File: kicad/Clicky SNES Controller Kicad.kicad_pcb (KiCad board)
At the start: 2 copper layers, 41.9 x 44.8 mm, 39 parts, among them CN1 CN1, P11 TL_IN, P13 TR_IN, P2 VSS_Trigger, P3 TR_TL_OUT, P4 DPAD_IN, P6 ABXY_IN, U1 4021, U2 4021, X1 SW_PUSH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

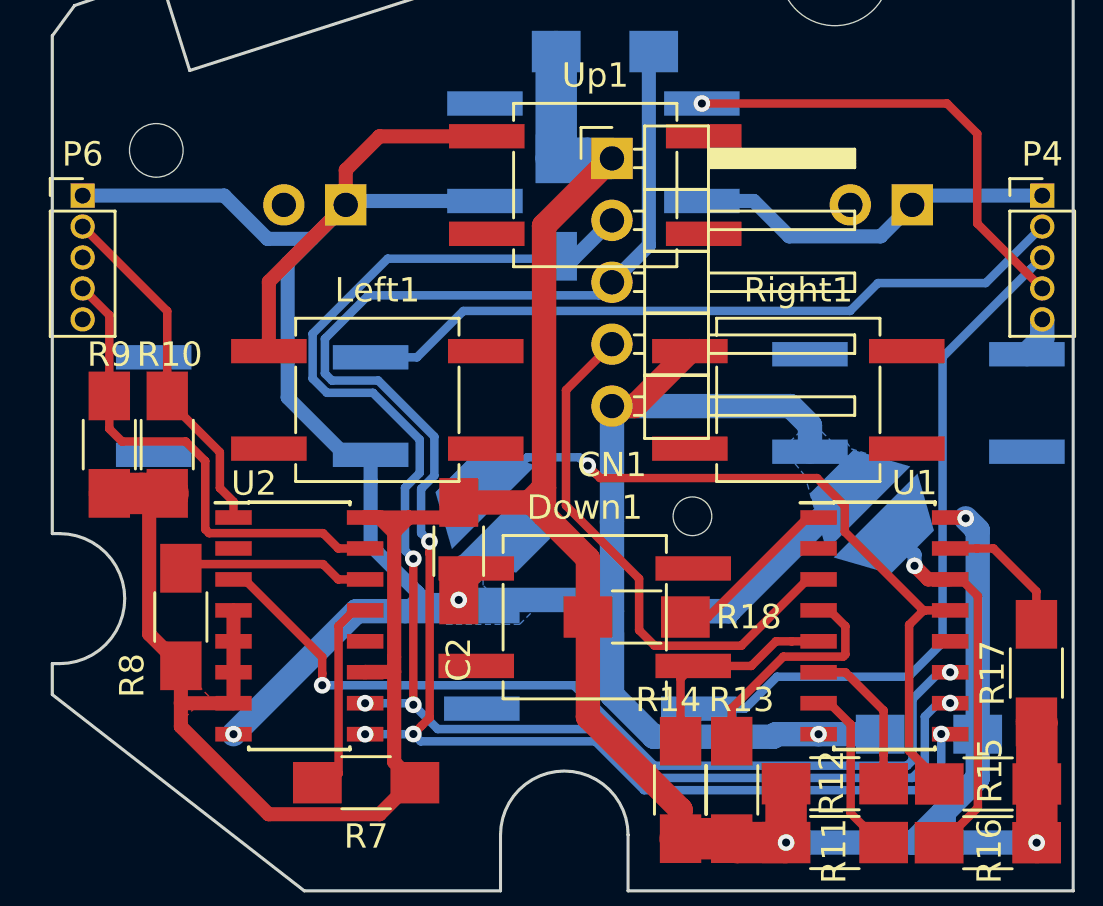
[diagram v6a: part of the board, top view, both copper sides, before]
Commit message: PCB: Route ABXY_IN pins
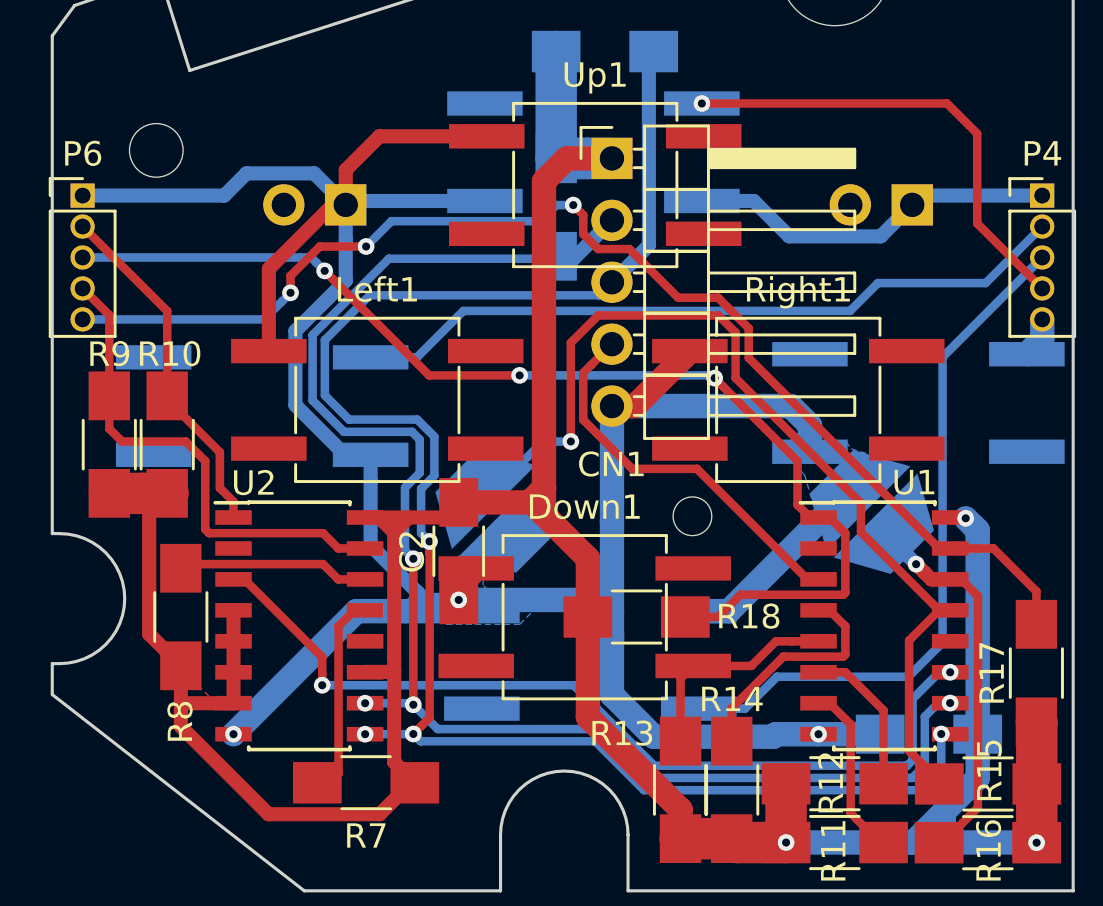
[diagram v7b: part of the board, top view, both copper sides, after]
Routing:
- net /Y: track 5.62 -> 50.6 mm, vias 0 -> 3
- net /B: track 7.15 -> 47.4 mm, vias 0 -> 3
- net /Start: track 30.9 -> 39.5 mm
- net /SEROUT: track 22.5 -> 16.0 mm
- net GND: track 147.2 -> 148.8 mm
- net +5V: track 130.8 -> 131.8 mm

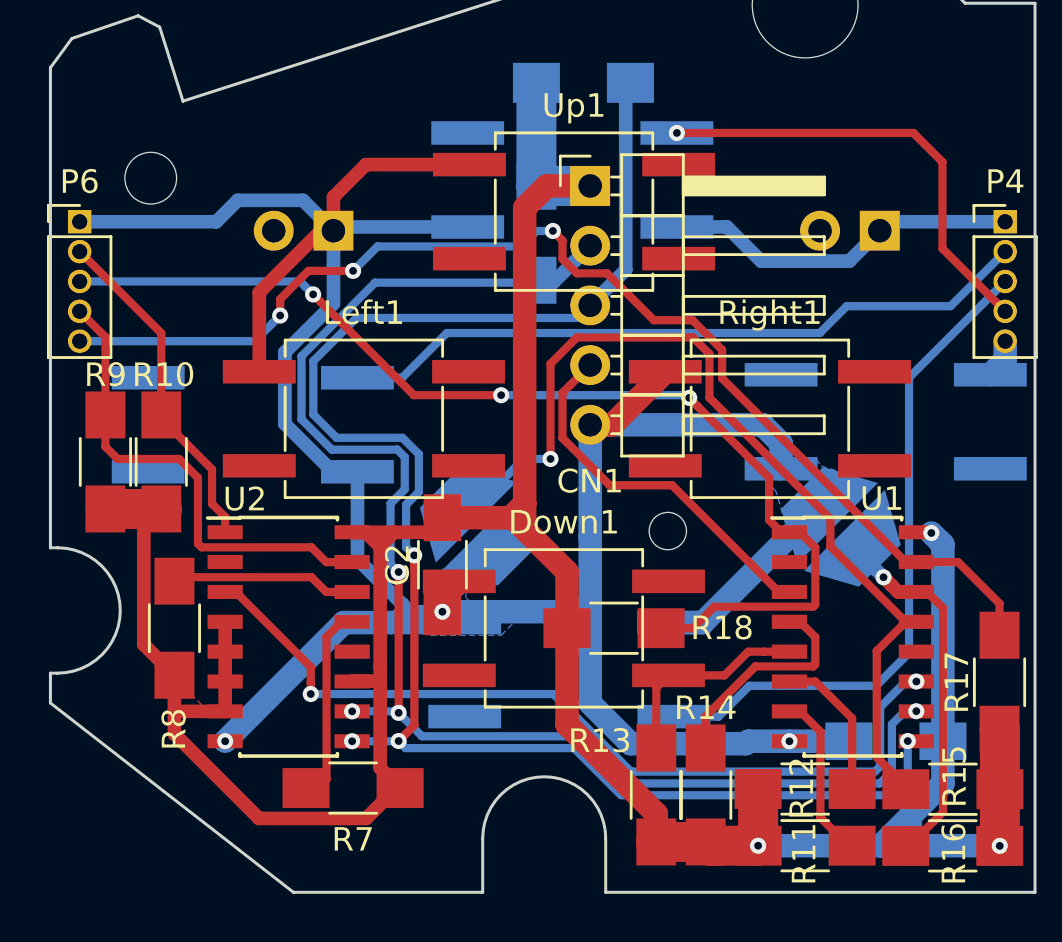
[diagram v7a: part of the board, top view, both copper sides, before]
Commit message: PCB: Route TR/TL jumper pins
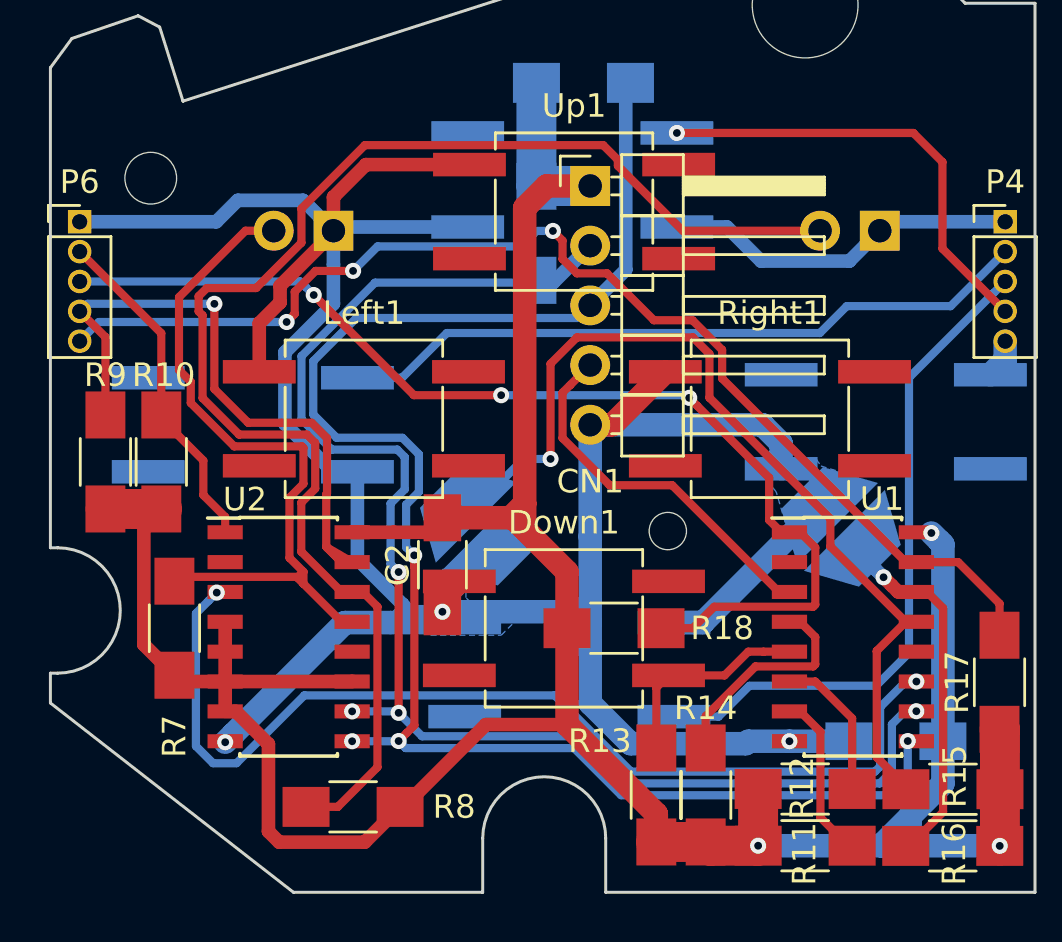
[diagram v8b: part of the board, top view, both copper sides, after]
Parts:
- moved R8 10.7 mm to (25.6, 54.1), turned to 0 degrees
- moved R7 10.2 mm to (18.0, 46.5), turned to 270 degrees
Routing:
- net /TL: track 7.89 -> 61.2 mm
- net /TR: track 8.44 -> 31.0 mm
- net /X: track 20.4 -> 28.3 mm, vias 0 -> 1
- net Net-(U1-Pad11): track 36.3 -> 43.4 mm
- net +5V: track 131.8 -> 130.8 mm
- removed copper zone on F.Cu, net +5V
